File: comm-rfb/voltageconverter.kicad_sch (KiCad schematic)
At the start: 6 parts

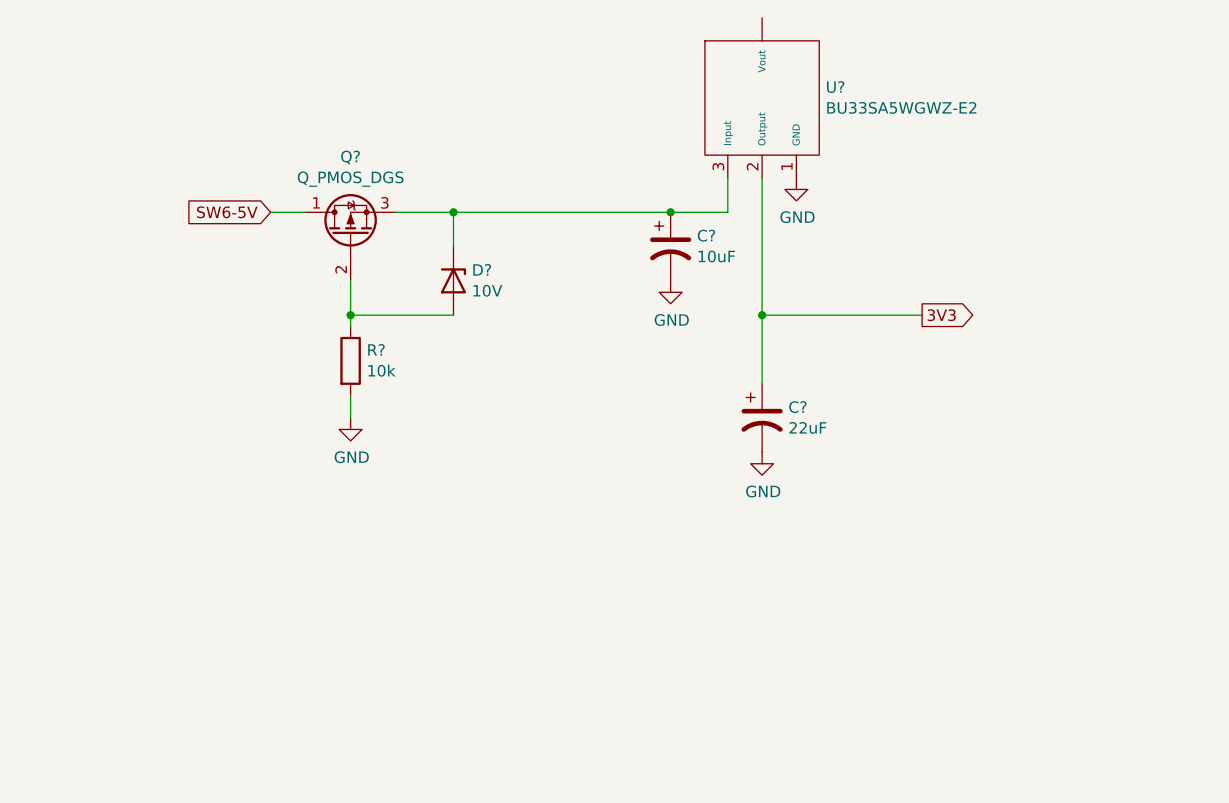
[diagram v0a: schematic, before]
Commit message: updated voltage converter
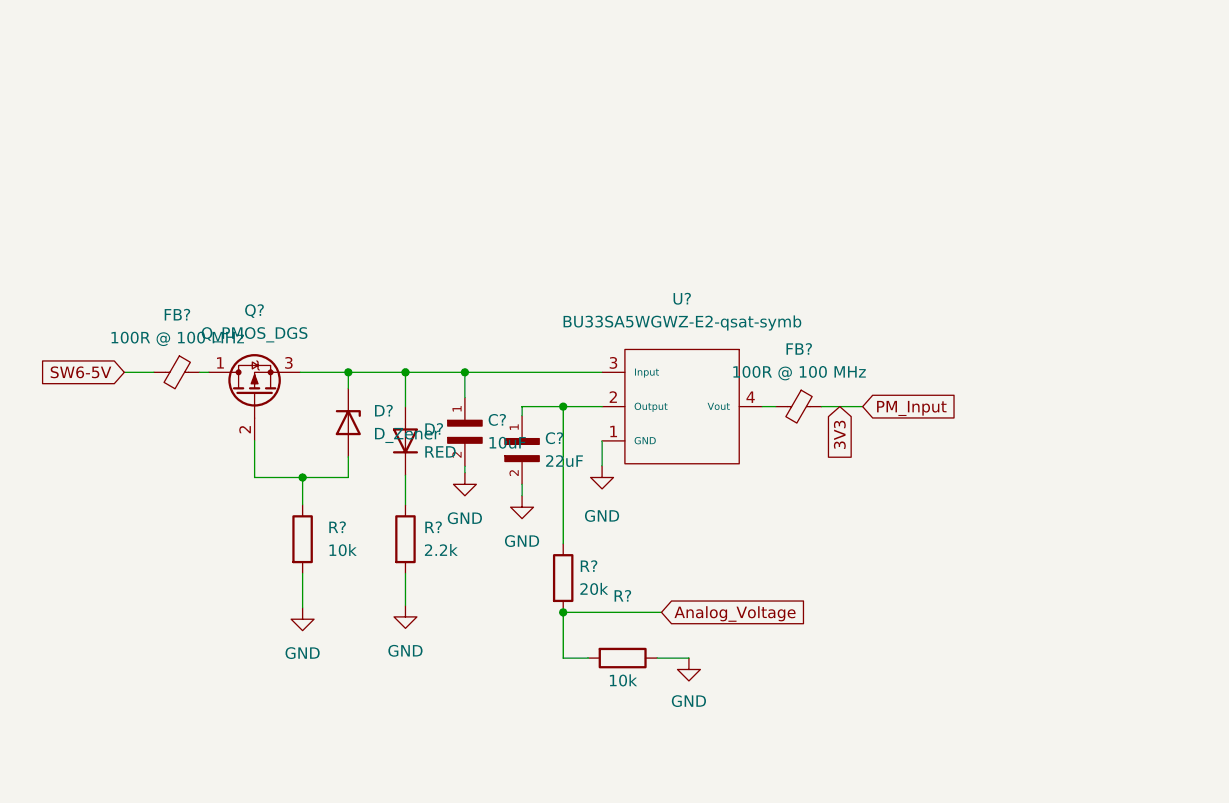
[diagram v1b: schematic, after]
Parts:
- removed C?: 10uF, symbol qsat5to3.3-rescue:CP1-Device
- removed C?: 22uF, symbol qsat5to3.3-rescue:CP1-Device
- removed D?: 10V, Package_TO_SOT_SMD:SOT-23, symbol Device:D_Zener
- removed Q?: Q_PMOS_DGS, symbol Device:Q_PMOS_DGS
- removed R?: 10k, symbol Device:R
- removed U?: BU33SA5WGWZ-E2, qsat5to3:BU33SA5WGWZ-E2, symbol qsat5to3.3-rescue:BU33SA5WGWZ-E2-qsat-symb
- added C?: 22uF, CAPC1608X90N, symbol Daughterboard_Symbols:CL10B104KB8NNNL
- added C?: 10uF, CAPC1608X90N, symbol Daughterboard_Symbols:CL10B104KB8NNNL
- added D?: D_Zener, STM32_Breakout:SOT91P240X110-3N, symbol Device:D_Zener
- added D?: RED, Daughterboard_footprints:CAPC1608X90N, symbol Simulation_SPICE:DIODE
- added FB? (x2): 100R @ 100 MHz, Daughterboard_footprints:BEADC1608X75N, symbol Device:FerriteBead_Small
- added Q?: Q_PMOS_DGS, STM32_Breakout:SOT91P240X110-3N, symbol Device:Q_PMOS_DGS
- added R?: 20k, Daughterboard_footprints:RESC1608X55N, symbol Device:R
- added R? (x2): 10k, Daughterboard_footprints:RESC1608X55N, symbol Device:R
- added R?: 2.2k, Daughterboard_footprints:RESC1608X55N, symbol Device:R
- added U?: BU33SA5WGWZ-E2-qsat-symb, STM32_Breakout:BU33SA5WGWZ-E2, symbol Imported_OBC_Library:BU33SA5WGWZ-E2-qsat-symb
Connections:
- net 3V3: now also FB?.1
- net GND: now also C?.2, C?.2, R?.1, R?.2, R?.2, U?.1 (GND)
- net SW6-5V: now also FB?.2
- new net: C?.1, D?.1 (A), D?.1 (K), Q?.3 (S), U?.3 (Input)
- new net: D?.2 (A), Q?.2 (G), R?.1
- new net: C?.1, R?.1, U?.2 (Output)
- new net: FB?.2, U?.4 (Vout)
- new net: FB?.1, Q?.1 (D)
- new net: D?.2 (K), R?.1
- new net Analog_Voltage: R?.2, R?.2

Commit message: updated voltage converter
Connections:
- net 3V3: no longer FB?.1
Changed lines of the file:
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@@
     )
   )
-  (global_label "PM_Input" (shape input) (at 176.276 92.71 0) (fields_autoplaced)
-    (effects (font (size 1.27 1.27)) (justify left))
-    (property "Intersheet References" "${INTERSHEET_REFS}" (id 0) (at 187.1558 92.6306 0)
-      (effects (font (size 1.27 1.27)) (justify left) hide)
-    )
-  )
-  (global_label "3V3" (shape input) (at 173.736 92.71 270) (fields_autoplaced)
+  (global_label "3V3" (shape input) (at 176.53 92.71 270) (fields_autoplaced)
     (effects (font (size 1.27 1.27)) (justify right))
-    (property "Intersheet References" "${INTERSHEET_REFS}" (id 0) (at 173.6566 98.6307 90)
+    (property "Intersheet References" "${INTERSHEET_REFS}" (id 0) (at 176.4506 98.6307 90)
       (effects (font (size 1.27 1.27)) (justify right) hide)
     )

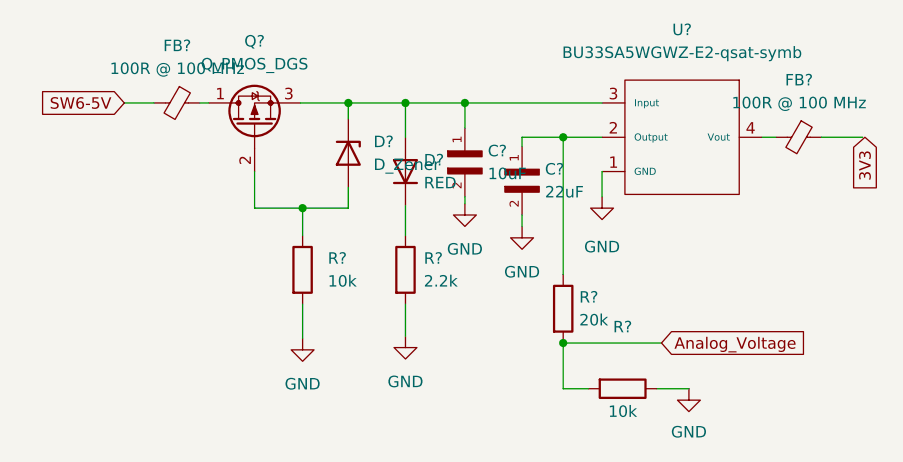
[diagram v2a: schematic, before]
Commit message: comm-rfb: reformat main schematic page
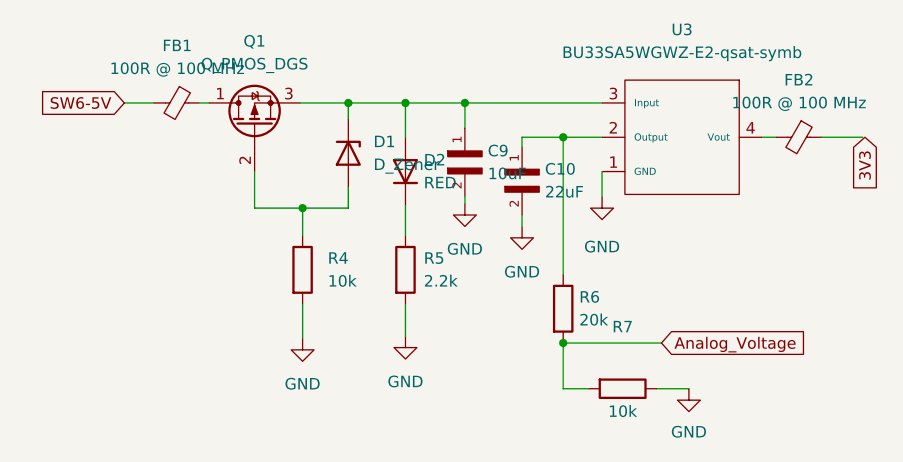
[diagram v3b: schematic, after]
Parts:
- gave numbers to parts that had none: 12
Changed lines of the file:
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@@
   (symbol (lib_id "Device:D_Zener") (at 119.126 94.488 270) (unit 1)
     (in_bom yes) (on_board yes) (fields_autoplaced)
-    (property "Reference" "D?" (id 0) (at 121.92 93.2179 90)
+    (property "Reference" "D1" (id 0) (at 121.92 93.2179 90)
       (effects (font (size 1.27 1.27)) (justify left))
     )
@@
   (symbol (lib_id "Daughterboard_Symbols:CL10B104KB8NNNL") (at 138.43 96.266 270) (unit 1)
     (in_bom yes) (on_board yes) (fields_autoplaced)
-    (property "Reference" "C?" (id 0) (at 140.97 96.2659 90)
+    (property "Reference" "C10" (id 0) (at 140.97 96.2659 90)
       (effects (font (size 1.27 1.27)) (justify left))
     )
@@
   (symbol (lib_id "Imported_OBC_Library:BU33SA5WGWZ-E2-qsat-symb") (at 156.21 92.71 270) (unit 1)
     (in_bom yes) (on_board yes) (fields_autoplaced)
-    (property "Reference" "U?" (id 0) (at 156.21 80.772 90))
+    (property "Reference" "U3" (id 0) (at 156.21 80.772 90))
     (property "Value" "BU33SA5WGWZ-E2-qsat-symb" (id 1) (at 156.21 83.312 90))
     (property "Footprint" "STM32_Breakout:BU33SA5WGWZ-E2" (id 2) (at 156.21 92.71 0)
@@
   (symbol (lib_id "power:GND") (at 138.43 102.616 0) (unit 1)
     (in_bom yes) (on_board yes) (fields_autoplaced)
-    (property "Reference" "#PWR?" (id 0) (at 138.43 108.966 0)
+    (property "Reference" "#PWR016" (id 0) (at 138.43 108.966 0)
       (effects (font (size 1.27 1.27)) hide)
     )
@@
   (symbol (lib_id "Device:FerriteBead_Small") (at 100.076 88.9 270) (unit 1)
     (in_bom yes) (on_board yes) (fields_autoplaced)
-    (property "Reference" "FB?" (id 0) (at 100.1141 82.55 90))
+    (property "Reference" "FB1" (id 0) (at 100.1141 82.55 90))
     (property "Value" "100R @ 100 MHz" (id 1) (at 100.1141 85.09 90))
     (property "Footprint" "Daughterboard_footprints:BEADC1608X75N" (id 2) (at 100.076 87.122 90)
@@
   (symbol (lib_id "Device:R") (at 143.002 111.76 0) (unit 1)
     (in_bom yes) (on_board yes) (fields_autoplaced)
-    (property "Reference" "R?" (id 0) (at 144.78 110.4899 0)
+    (property "Reference" "R6" (id 0) (at 144.78 110.4899 0)
       (effects (font (size 1.27 1.27)) (justify left))
     )
@@
   (symbol (lib_id "power:GND") (at 156.972 120.65 0) (unit 1)
     (in_bom yes) (on_board yes) (fields_autoplaced)
-    (property "Reference" "#PWR?" (id 0) (at 156.972 127 0)
+    (property "Reference" "#PWR018" (id 0) (at 156.972 127 0)
       (effects (font (size 1.27 1.27)) hide)
     )
@@
   (symbol (lib_id "power:GND") (at 132.08 100.076 0) (unit 1)
     (in_bom yes) (on_board yes) (fields_autoplaced)
-    (property "Reference" "#PWR?" (id 0) (at 132.08 106.426 0)
+    (property "Reference" "#PWR015" (id 0) (at 132.08 106.426 0)
       (effects (font (size 1.27 1.27)) hide)
     )
@@
   (symbol (lib_id "Daughterboard_Symbols:CL10B104KB8NNNL") (at 132.08 94.234 270) (unit 1)
     (in_bom yes) (on_board yes) (fields_autoplaced)
-    (property "Reference" "C?" (id 0) (at 134.62 94.2339 90)
+    (property "Reference" "C9" (id 0) (at 134.62 94.2339 90)
       (effects (font (size 1.27 1.27)) (justify left))
     )
@@
   (symbol (lib_id "Device:R") (at 114.046 107.442 0) (unit 1)
     (in_bom yes) (on_board yes) (fields_autoplaced)
-    (property "Reference" "R?" (id 0) (at 116.84 106.1719 0)
+    (property "Reference" "R4" (id 0) (at 116.84 106.1719 0)
       (effects (font (size 1.27 1.27)) (justify left))
     )
@@
   (symbol (lib_id "power:GND") (at 125.476 114.808 0) (unit 1)
     (in_bom yes) (on_board yes) (fields_autoplaced)
-    (property "Reference" "#PWR?" (id 0) (at 125.476 121.158 0)
+    (property "Reference" "#PWR014" (id 0) (at 125.476 121.158 0)
       (effects (font (size 1.27 1.27)) hide)
     )
@@
   (symbol (lib_id "Device:Q_PMOS_DGS") (at 108.712 91.44 90) (unit 1)
     (in_bom yes) (on_board yes) (fields_autoplaced)
-    (property "Reference" "Q?" (id 0) (at 108.712 82.042 90))
+    (property "Reference" "Q1" (id 0) (at 108.712 82.042 90))
     (property "Value" "Q_PMOS_DGS" (id 1) (at 108.712 84.582 90))
     (property "Footprint" "STM32_Breakout:SOT91P240X110-3N" (id 2) (at 106.172 86.36 0)
@@
   (symbol (lib_id "Device:R") (at 149.606 120.65 270) (unit 1)
     (in_bom yes) (on_board yes)
-    (property "Reference" "R?" (id 0) (at 149.606 113.792 90))
+    (property "Reference" "R7" (id 0) (at 149.606 113.792 90))
     (property "Value" "10k" (id 1) (at 149.606 123.19 90))
     (property "Footprint" "Daughterboard_footprints:RESC1608X55N" (id 2) (at 149.606 118.872 90)
@@
   (symbol (lib_id "power:GND") (at 114.046 115.062 0) (unit 1)
     (in_bom yes) (on_board yes) (fields_autoplaced)
-    (property "Reference" "#PWR?" (id 0) (at 114.046 121.412 0)
+    (property "Reference" "#PWR013" (id 0) (at 114.046 121.412 0)
       (effects (font (size 1.27 1.27)) hide)
     )
@@
   (symbol (lib_id "Device:FerriteBead_Small") (at 169.164 92.71 270) (unit 1)
     (in_bom yes) (on_board yes) (fields_autoplaced)
-    (property "Reference" "FB?" (id 0) (at 169.2021 86.36 90))
+    (property "Reference" "FB2" (id 0) (at 169.2021 86.36 90))
     (property "Value" "100R @ 100 MHz" (id 1) (at 169.2021 88.9 90))
     (property "Footprint" "Daughterboard_footprints:BEADC1608X75N" (id 2) (at 169.164 90.932 90)
@@
   (symbol (lib_id "Device:R") (at 125.476 107.442 0) (unit 1)
     (in_bom yes) (on_board yes) (fields_autoplaced)
-    (property "Reference" "R?" (id 0) (at 127.508 106.1719 0)
+    (property "Reference" "R5" (id 0) (at 127.508 106.1719 0)
       (effects (font (size 1.27 1.27)) (justify left))
     )
@@
   (symbol (lib_id "Simulation_SPICE:DIODE") (at 125.476 96.52 270) (unit 1)
     (in_bom yes) (on_board yes) (fields_autoplaced)
-    (property "Reference" "D?" (id 0) (at 127.508 95.2499 90)
+    (property "Reference" "D2" (id 0) (at 127.508 95.2499 90)
       (effects (font (size 1.27 1.27)) (justify left))
     )
@@
   (symbol (lib_id "power:GND") (at 147.32 99.314 0) (unit 1)
     (in_bom yes) (on_board yes) (fields_autoplaced)
-    (property "Reference" "#PWR?" (id 0) (at 147.32 105.664 0)
-      (effects (font (size 1.27 1.27)) hide)
-    )
+    (property "Reference" "#PWR017" (id 0) (at 147.32 105.664 0)
+      (effects (font (size 1.27 1.27)) hide)
+    )

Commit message: comm-rfb: reduce number of sheets in schematic
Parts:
- removed C10: 22uF, CAPC1608X90N, symbol Daughterboard_Symbols:CL10B104KB8NNNL
- removed C9: 10uF, CAPC1608X90N, symbol Daughterboard_Symbols:CL10B104KB8NNNL
- removed D1: D_Zener, STM32_Breakout:SOT91P240X110-3N, symbol Device:D_Zener
- removed D2: RED, Daughterboard_footprints:CAPC1608X90N, symbol Simulation_SPICE:DIODE
- removed FB2: 100R @ 100 MHz, Daughterboard_footprints:BEADC1608X75N, symbol Device:FerriteBead_Small
- removed Q1: Q_PMOS_DGS, STM32_Breakout:SOT91P240X110-3N, symbol Device:Q_PMOS_DGS
- removed R6: 20k, Daughterboard_footprints:RESC1608X55N, symbol Device:R
- removed R7: 10k, Daughterboard_footprints:RESC1608X55N, symbol Device:R
- removed U3: BU33SA5WGWZ-E2-qsat-symb, STM32_Breakout:BU33SA5WGWZ-E2, symbol Imported_OBC_Library:BU33SA5WGWZ-E2-qsat-symb
- added C19: 100n, Capacitor_SMD:C_0603_1608Metric, symbol Device:C
- added C20, C21: 22u, Capacitor_SMD:C_0805_2012Metric, symbol Device:C
- added D1: LED, LED_SMD:LED_0603_1608Metric, symbol Device:LED
- added MAX4372F1: MAX4372FESA+, STM32_Breakout:SOIC127P600X175-8N, symbol STM32_Breakout-rescue:MAX4372FESA+-MAX4372FESA+
- added TP1: TestPoint, TestPoint:TestPoint_Pad_D2.0mm, symbol Connector:TestPoint
- added U3: AMS1117-3.3, Package_TO_SOT_SMD:SOT-223-3_TabPin2, symbol Regulator_Linear:AMS1117-3.3
- FB1: footprint Daughterboard_footprints:BEADC1608X75N -> Inductor_SMD:L_0603_1608Metric
- R4: value 10k -> 1k5; footprint Daughterboard_footprints:RESC1608X55N -> Resistor_SMD:R_0603_1608Metric
- R5: value 2.2k -> 100m; footprint Daughterboard_footprints:RESC1608X55N -> Resistor_SMD:R_0603_1608Metric
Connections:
- net GND: now also R4.1, C19.2, C20.2, C21.2, MAX4372F1.3 (GND), U3.1 (GND); no longer R4.2, R5.2
- net SW6-5V: now also C19.1, MAX4372F1.1 (VCC)
- net at FB1.1: now also C20.1, U3.3 (VI)
- net VCC_3V3: now reaches R5.1
- net VCC_3V3: now also C21.1, D1.2 (A), MAX4372F1.8 (RS+), U3.2 (VO)
- new net: D1.1 (K), R4.2
- new net +3V3: MAX4372F1.6 (RS-), R5.2, TP1.1
- new net CURR-MONITOR: MAX4372F1.4 (OUT)
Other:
- note added: "3V3 Low Dropout Voltage Regulator"
- moved on the sheet: FB1

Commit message: comm-rfb: include correct spacing for cc1120-em connectors, remove traces
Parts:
- removed TP1: TestPoint, TestPoint:TestPoint_Pad_D2.0mm, symbol Connector:TestPoint
- C20, C21: footprint Capacitor_SMD:C_0805_2012Metric -> Capacitor_SMD:C_0603_1608Metric
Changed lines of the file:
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@@
   (junction (at 161.29 74.295) (diameter 0) (color 0 0 0 0)
-  )
-  (junction (at 207.645 128.27) (diameter 0) (color 0 0 0 0)
   )
   (junction (at 107.315 116.205) (diameter 0) (color 0 0 0 0)
@@
       (effects (font (size 1.27 1.27)) (justify left))
     )
-    (property "Footprint" "Capacitor_SMD:C_0805_2012Metric" (id 2) (at 134.3152 84.455 0)
+    (property "Footprint" "Capacitor_SMD:C_0603_1608Metric" (id 2) (at 134.3152 84.455 0)
       (effects (font (size 1.27 1.27)) hide)
     )
@@
     (pin "1")
     (pin "2")
-  )
-  (symbol (lib_id "Connector:TestPoint") (at 207.645 128.27 180) (unit 1)
-    (in_bom yes) (on_board yes)
-    (property "Reference" "TP1" (id 0) (at 208.915 130.81 0)
-      (effects (font (size 1.27 1.27)) (justify right))
-    )
-    (property "Value" "TestPoint" (id 1) (at 203.835 133.35 0)
-      (effects (font (size 1.27 1.27)) (justify right))
-    )
-    (property "Footprint" "TestPoint:TestPoint_Pad_D2.0mm" (id 2) (at 202.565 128.27 0)
-      (effects (font (size 1.27 1.27)) hide)
-    )
-    (property "Datasheet" "~" (id 3) (at 202.565 128.27 0)
-      (effects (font (size 1.27 1.27)) hide)
-    )
-    (pin "1")
   )
   (symbol (lib_id "Device:C") (at 107.315 121.285 0) (unit 1)
@@
       (effects (font (size 1.27 1.27)) (justify left))
     )
-    (property "Footprint" "Capacitor_SMD:C_0805_2012Metric" (id 2) (at 162.2552 84.455 0)
-      (effects (font (size 1.27 1.27)) hide)
-    )
+    (property "Footprint" "Capacitor_SMD:C_0603_1608Metric" (id 2) (at 162.2552 84.455 0)
+      (effects (font (size 1.27 1.27)) hide)
+    )
